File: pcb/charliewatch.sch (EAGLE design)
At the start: 85 parts, among them U2 CC430F5137IRGZR, X1 CRYSTALS-NOGND-IQXC-25, X2 FA-128

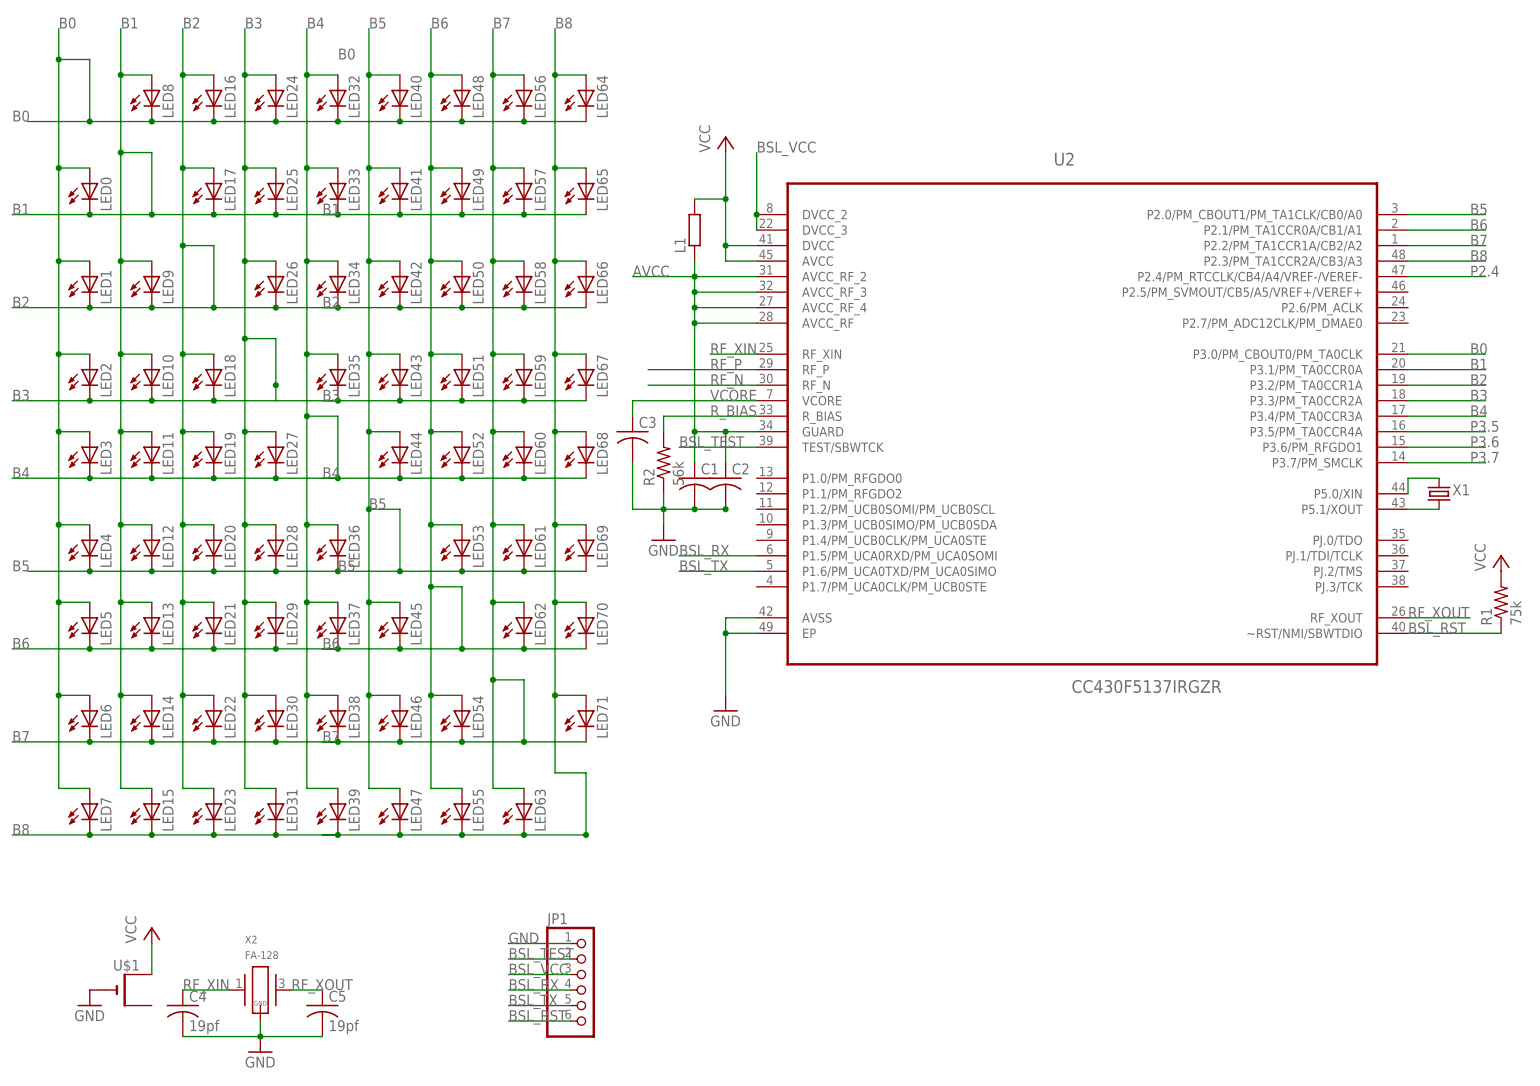
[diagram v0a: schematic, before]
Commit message: Add LIS3DH Accelerometer
LIS3DH is an i2c accelerometer. Hope to use this to control the watch
with tap based gestures
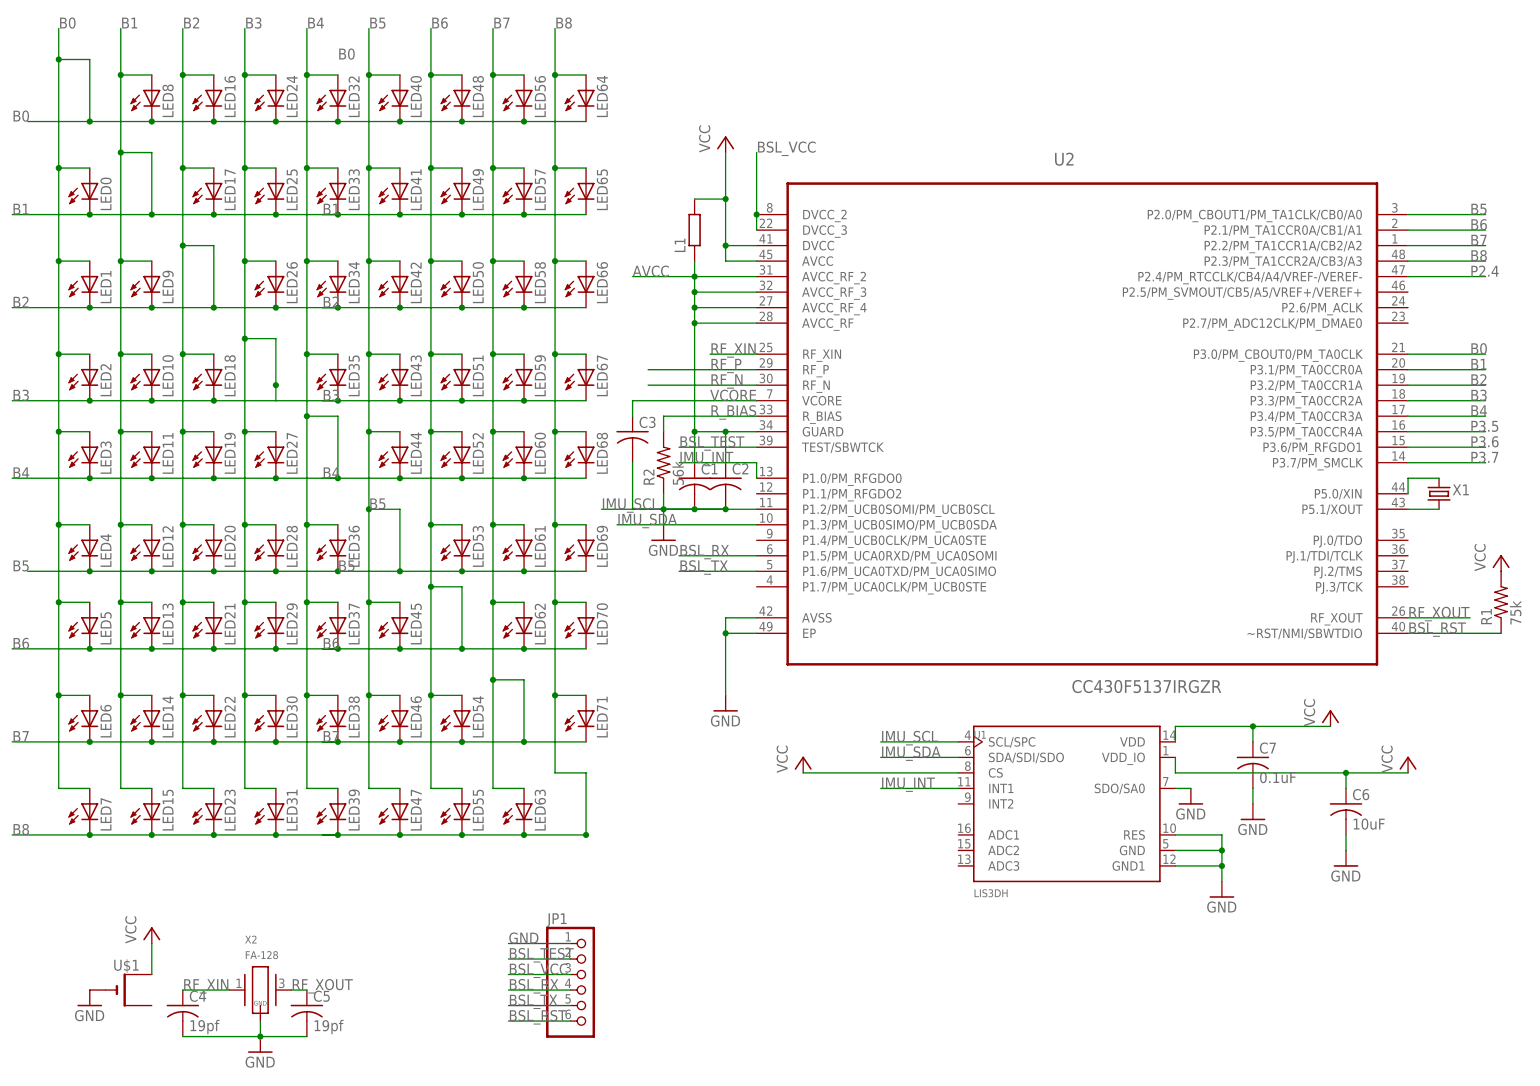
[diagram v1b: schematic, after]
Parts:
- added C6: 10uF, resistor:C-USC0603
- added C7: 0.1uF, resistor:C-USC0603
- added U1: LIS3DH, LIS3DH:LIS3DH
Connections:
- new net IMU_INT: U1.INT1, U2.P1.0/PM_RFGDO0
- new net IMU_SCL: U1.SCL/SPC, U2.P1.2/PM_UCB0SOMI/PM_UCB0SCL
- new net IMU_SDA: U1.SDA/SDI/SDO, U2.P1.3/PM_UCB0SIMO/PM_UCB0SDA
- net GND: now also C6.2, C7.2, U1.GND, U1.GND1, U1.RES, U1.SDO/SA0
- net VCC: now also C6.1, C7.1, U1.CS, U1.VDD, U1.VDD_IO
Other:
- moved on the sheet: C5
